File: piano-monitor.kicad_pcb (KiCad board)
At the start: 2 copper layers, 166 x 72.3 mm, 7 parts, among them J3 NCJ6FA-V, J4 DC, J7 NCJ6FA-V

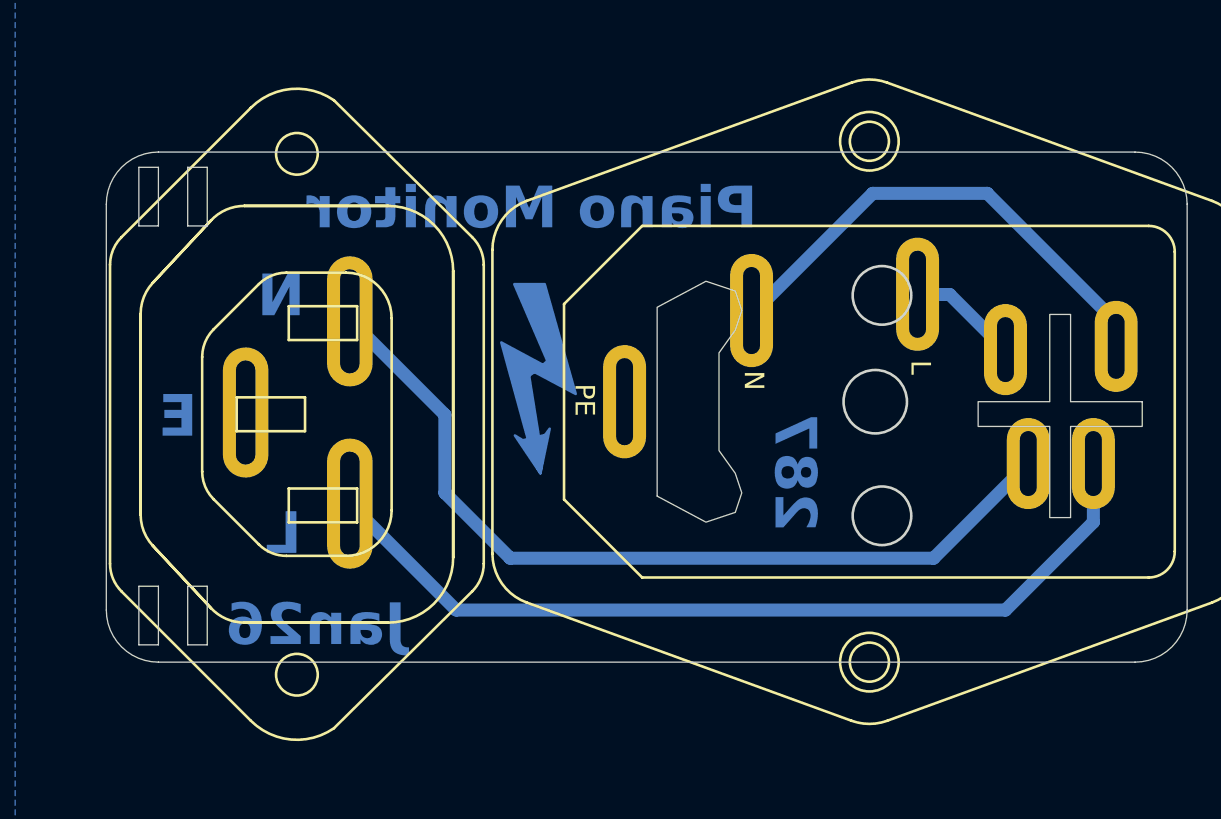
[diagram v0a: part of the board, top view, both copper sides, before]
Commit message: Update AC footprints
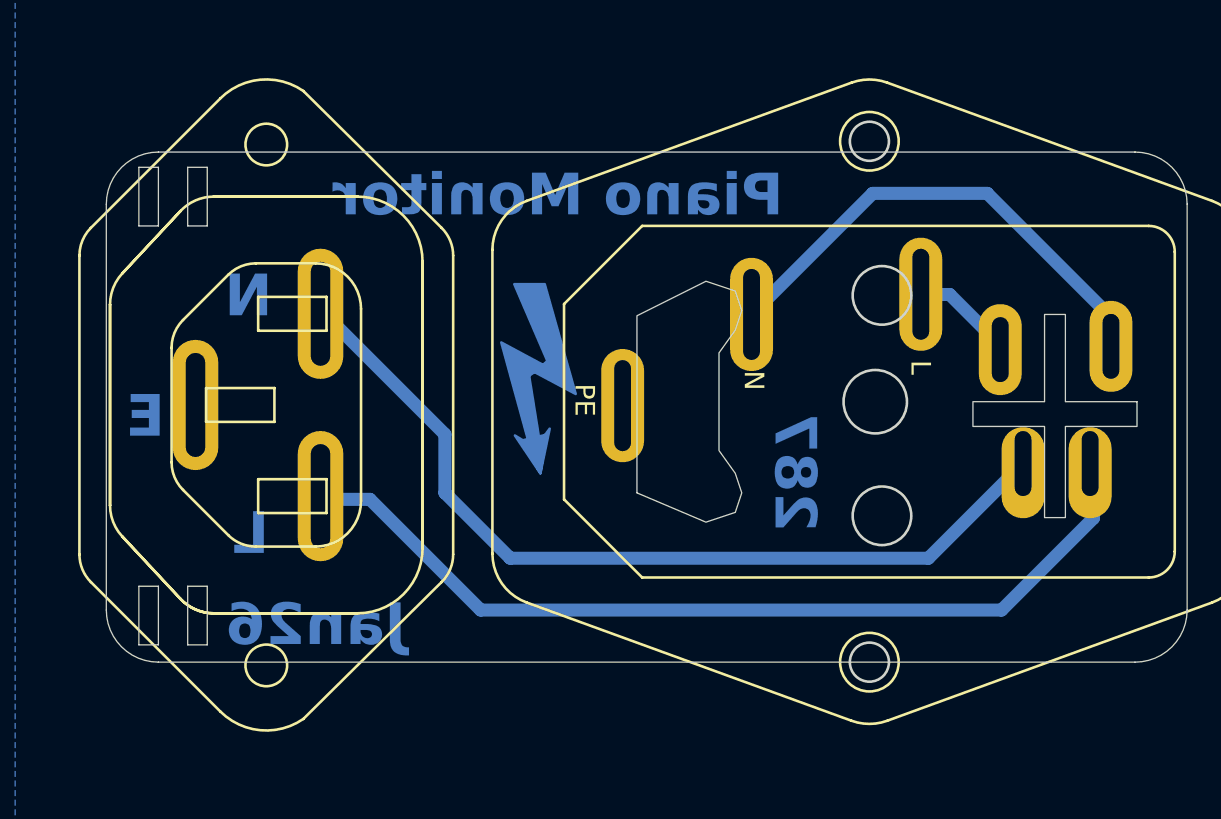
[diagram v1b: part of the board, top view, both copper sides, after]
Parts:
- moved J6 2.46 mm to (208.2, 96.2)
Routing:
- net L: track 67.8 -> 70.1 mm
- net N: track 66.2 -> 67.8 mm
